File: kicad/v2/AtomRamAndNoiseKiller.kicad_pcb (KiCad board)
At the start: 2 copper layers, 76.2 x 49.5 mm, 27 parts, among them J1 Conn_01x10, J10 Conn_01x03, J2 Conn_01x10, J3 Conn_01x03, J4 Conn_01x09, J5 Conn_01x09, J6 Conn_01x03, J7 Conn_01x02, J8 Conn_01x01, J9 Conn_01x03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

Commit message: Final tweaks
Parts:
- removed J10, J9: Conn_01x03, Connector_PinHeader_2.54mm:PinHeader_1x03_P2.54mm_Vertical
- removed J8: Conn_01x01, Connector_PinHeader_2.54mm:PinHeader_1x01_P2.54mm_Horizontal
- added LK1: Conn_01x03, Connector_PinHeader_2.54mm:PinHeader_1x03_P2.54mm_Vertical, F.Cu at (204.5, 118.1)
- added LK2: Conn_01x03, Connector_PinHeader_2.54mm:PinHeader_1x03_P2.54mm_Vertical, F.Cu at (204.5, 128.3)
- added LK3: Conn_01x02, Connector_PinHeader_2.54mm:PinHeader_1x02_P2.54mm_Vertical, F.Cu at (205.7, 148.0)
- J7: value Conn_01x02 -> Conn_01x01; footprint Connector_PinHeader_2.54mm:PinHeader_1x02_P2.54mm_Vertical -> Connector_PinHeader_2.54mm:PinHeader_1x01_P2.54mm_Horizontal
- moved J7 5.12 mm to (210.2, 149.2), turned to 270 degrees
- moved R3 2.54 mm to (210.2, 143.5)
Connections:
- J7 pad 1: /LOAD -> /RRDISABLE
- U2 pad 8: Net-(J7-Pad2) -> Net-(LK3-Pad2)
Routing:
- net Net-(LK3-Pad2): track 0.00 -> 9.57 mm
- net Net-(J7-Pad2): track 8.04 -> 0.00 mm
- net /RRDISABLE: track 24.3 -> 27.5 mm
- net /LOAD: track 37.5 -> 38.8 mm
- net Net-(R1-Pad1): track 14.3 -> 15.4 mm
- net /A4: track 33.8 -> 34.4 mm
- net /A2: track 33.8 -> 34.4 mm
- net /A6: track 14.4 -> 14.9 mm

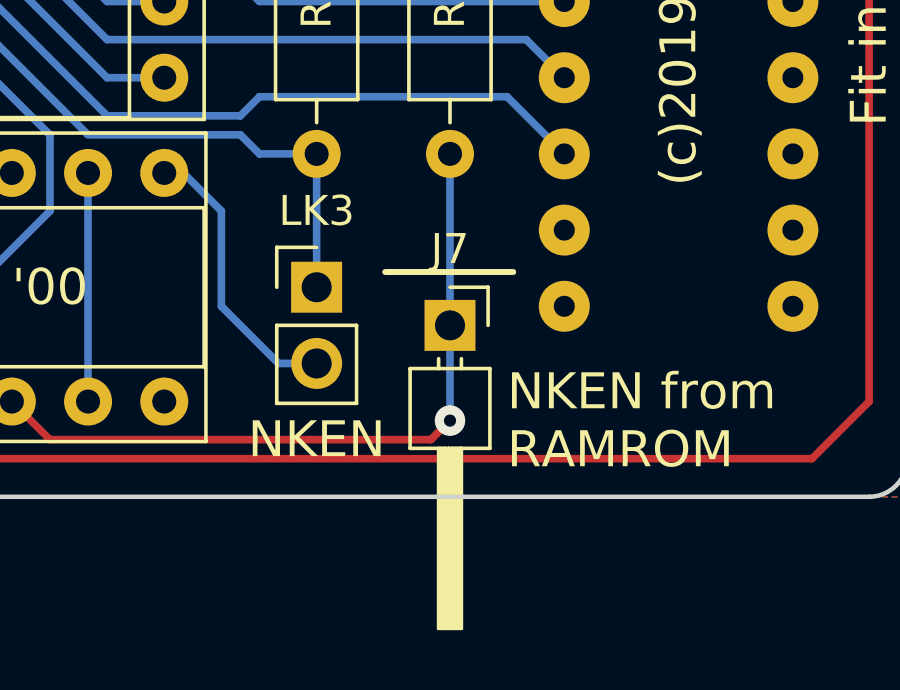
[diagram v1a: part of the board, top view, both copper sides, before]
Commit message: Moved J7 in a tad
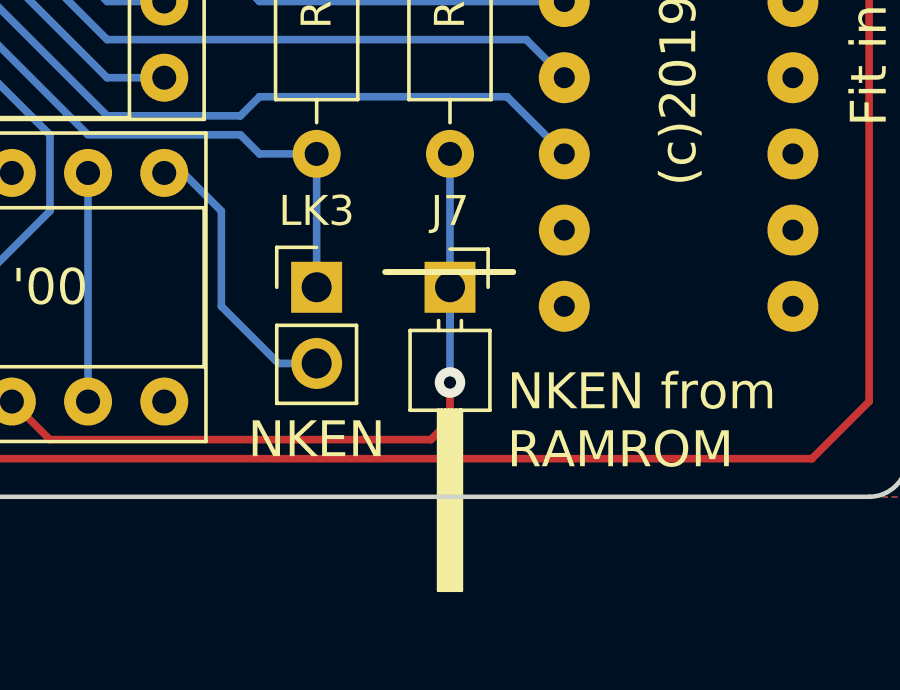
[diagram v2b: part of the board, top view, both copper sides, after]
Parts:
- moved J7 1.27 mm to (210.2, 148.0)
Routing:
- net /RRDISABLE: track 27.5 -> 28.7 mm
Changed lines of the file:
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@@
     (thickness 1.6)
     (drawings 43)
-    (tracks 371)
+    (tracks 372)
     (zones 0)
     (modules 27)
@@
   )
   (module Connector_PinHeader_2.54mm:PinHeader_1x01_P2.54mm_Horizontal (layer F.Cu)
-    (at 210.185 149.225 270)
+    (at 210.185 147.955 270)
     (descr "Through hole angled pin header, 1x01, 2.54mm pitch, 6mm pin length, single row")
     (tags "Through hole angled pin header THT 1x01 2.54mm single row")
@@
   (segment (start 195.58 151.765) (end 196.85 153.035) (width 0.254) (layer F.Cu) (net 3) (status 10))
   (segment (start 209.55 153.035) (end 210.185 152.4) (width 0.254) (layer F.Cu) (net 3))
-  (via (at 210.185 152.4) (size 1.016) (drill 0.4064) (layers F.Cu B.Cu) (net 3))
-  (segment (start 210.185 152.4) (end 210.185 149.225) (width 0.254) (layer B.Cu) (net 3) (status 20))
-  (segment (start 210.185 142.875) (end 210.185 149.225) (width 0.254) (layer B.Cu) (net 3) (status 30))
+  (via (at 210.185 151.13) (size 1.016) (drill 0.4064) (layers F.Cu B.Cu) (net 3))
+  (segment (start 210.185 151.13) (end 210.185 147.955) (width 0.254) (layer B.Cu) (net 3) (status 20))
+  (segment (start 210.185 142.875) (end 210.185 149.225) (width 0.254) (layer B.Cu) (net 3) (status 10))
+  (segment (start 210.185 152.4) (end 210.185 151.13) (width 0.254) (layer F.Cu) (net 3))
   (segment (start 178.435 133.35) (end 177.165 133.35) (width 0.254) (layer B.Cu) (net 4) (status 20))
   (segment (start 184.785 139.7) (end 178.435 133.35) (width 0.254) (layer B.Cu) (net 4))
